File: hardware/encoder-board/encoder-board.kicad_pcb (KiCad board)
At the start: 4 copper layers, 25.4 x 25.4 mm, 26 parts, among them J1 Conn_01x04, U1 ITR1204SR10A_TR(BY), U2 ITR1204SR10A_TR(BY), U3 LM2903

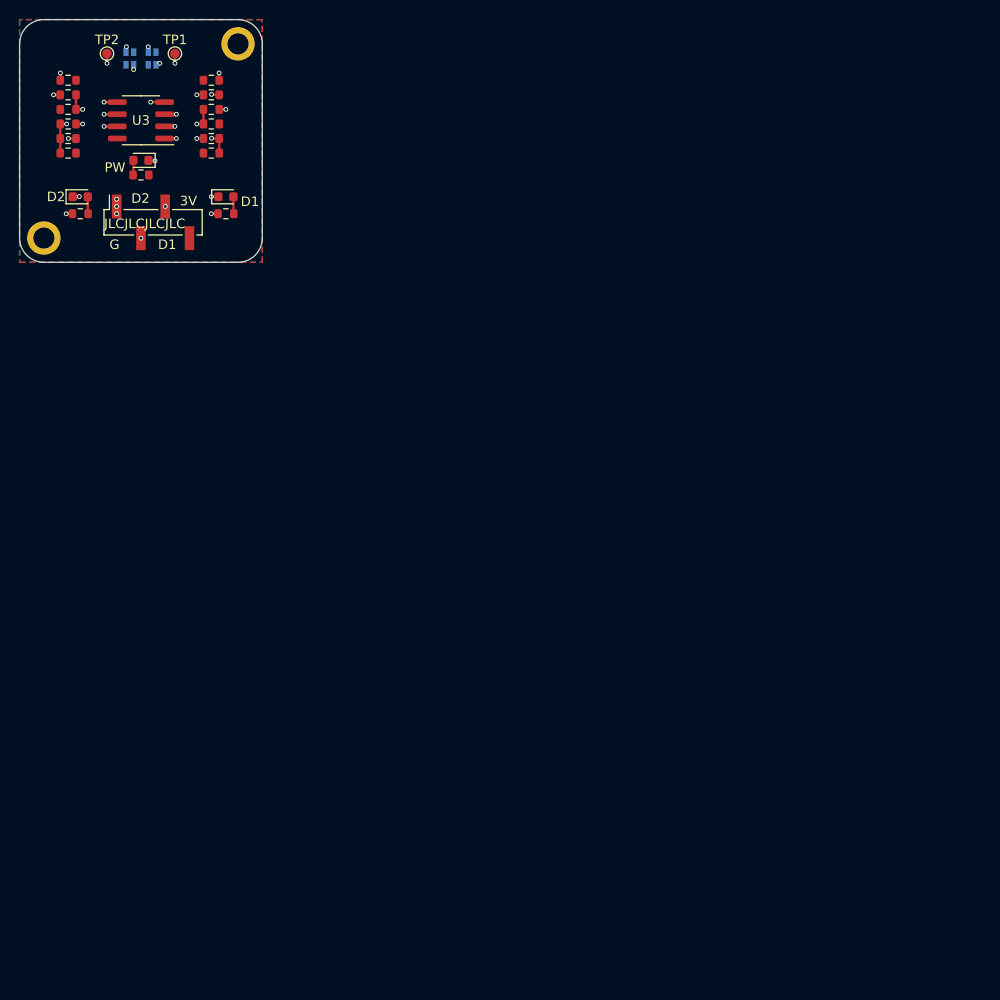
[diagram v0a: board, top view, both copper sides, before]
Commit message: remake encoder board pcb. generated jlcpcb production files.
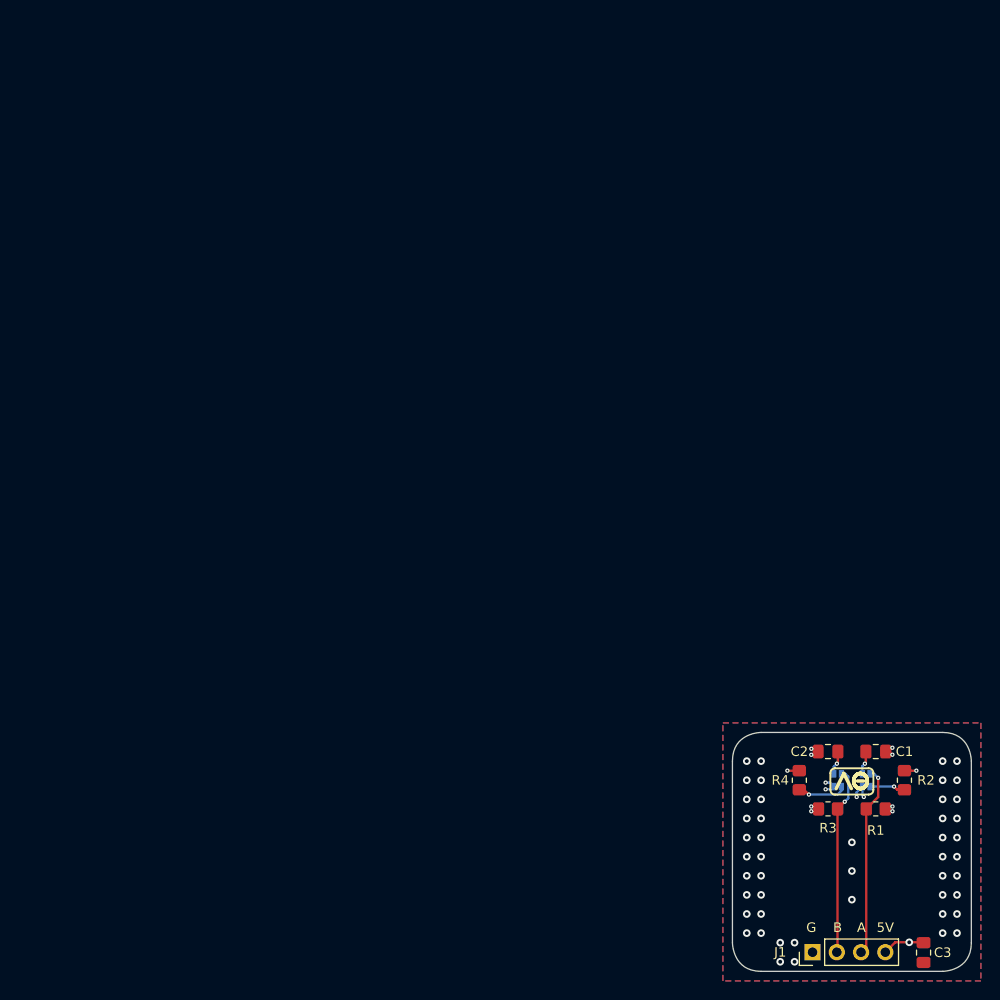
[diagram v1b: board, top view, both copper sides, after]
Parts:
- removed D1: Red, LED_SMD:LED_0603_1608Metric
- removed D2: Yellow, LED_SMD:LED_0603_1608Metric
- removed H1, H2: MountingHole_Pad, MountingHole:MountingHole_2.2mm_M2_ISO7380_Pad
- removed PW1: Green, LED_SMD:LED_0603_1608Metric
- removed R10, R11, R13, R14, R15, R8: 1k, Resistor_SMD:R_0603_1608Metric
- removed R12, R9: 1.5k, Resistor_SMD:R_0603_1608Metric
- removed R5: 30, Resistor_SMD:R_0603_1608Metric
- removed R6, R7: 130, Resistor_SMD:R_0603_1608Metric
- removed TP1, TP2: ~, TestPoint:TestPoint_Pad_D1.0mm
- removed U3: LM2903, Package_SO:SOIC-8_3.9x4.9mm_P1.27mm
- added C1: 100nF, Capacitor_SMD:C_0805_2012Metric_Pad1.18x1.45mm_HandSolder, F.Cu at (115.0, 102.0)
- added C2: 100nF, Capacitor_SMD:C_0805_2012Metric_Pad1.18x1.45mm_HandSolder, F.Cu at (110.0, 102.0)
- added C3: 10uF, Capacitor_SMD:C_0805_2012Metric_Pad1.18x1.45mm_HandSolder, F.Cu at (120.0, 123.0)
- J1: footprint Connector_PinHeader_2.54mm:PinHeader_1x04_P2.54mm_Vertical_SMD_Pin1Right -> Connector_PinHeader_2.54mm:PinHeader_1x04_P2.54mm_Vertical
- R1: value 1k -> 680; footprint Resistor_SMD:R_0603_1608Metric -> Resistor_SMD:R_0805_2012Metric_Pad1.20x1.40mm_HandSolder
- R2: renamed from R3; value 100 -> 390; footprint Resistor_SMD:R_0603_1608Metric -> Resistor_SMD:R_0805_2012Metric_Pad1.20x1.40mm_HandSolder
- R3: renamed from R2; value 1k -> 680; footprint Resistor_SMD:R_0603_1608Metric -> Resistor_SMD:R_0805_2012Metric_Pad1.20x1.40mm_HandSolder
- R4: value 100 -> 390; footprint Resistor_SMD:R_0603_1608Metric -> Resistor_SMD:R_0805_2012Metric_Pad1.20x1.40mm_HandSolder
- moved U1 106.3 mm to (114.0, 105.0), turned to 0 degrees
- moved R4 105.9 mm to (107.0, 105.0), turned to 90 degrees
- moved U2 105.8 mm to (111.0, 105.0), turned to 0 degrees
- moved R3 105.0 mm to (110.0, 108.0)
- moved R2 103.1 mm to (118.0, 105.0), turned to 90 degrees
- moved J1 102.9 mm to (108.4, 123.0)
- moved R1 97.7 mm to (115.0, 108.0)
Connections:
- J1 pad 2: D2 -> SENSE_B
- J1 pad 3: D1 -> SENSE_A
- J1 pad 4: +3V3 -> +5V
- R1 pad 1: +3V3 -> SENSE_A
- R1 pad 2: A1 -> GND
- R2 pad 2: +3V3 -> +5V
- R3 pad 1: +3V3 -> SENSE_B
- R3 pad 2: A2 -> GND
- R4 pad 2: +3V3 -> +5V
- U1 pad 1: A1 -> +5V
- U1 pad 2: GND -> SENSE_A
- U2 pad 1: A2 -> +5V
- U2 pad 2: GND -> SENSE_B
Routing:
- net D2: track 24.0 -> 0.00 mm, vias 4 -> 0
- net SENSE_A: track 0.00 -> 20.0 mm, vias 0 -> 1
- net SENSE_B: track 0.00 -> 19.7 mm, vias 0 -> 1
- net A2: track 18.2 -> 0.00 mm, vias 3 -> 0
- net D1: track 17.6 -> 0.00 mm, vias 4 -> 0
- net A1: track 16.9 -> 0.00 mm, vias 4 -> 0
- net +5V: track 0.00 -> 11.9 mm, vias 0 -> 5
- net GND: track 4.30 -> 11.3 mm, vias 9 -> 59
- net Net-(U1-A): track 10.4 -> 3.74 mm, vias 2 -> 1
- net Net-(U3B-+): track 6.16 -> 0.00 mm, vias 2 -> 0
- net Net-(U3A--): track 5.70 -> 0.00 mm, vias 2 -> 0
- net Net-(U2-A): track 10.4 -> 5.21 mm, vias 2 -> 1
- net Net-(U3A-+): track 4.91 -> 0.00 mm, vias 2 -> 0
- net Net-(U3B--): track 4.74 -> 0.00 mm, vias 2 -> 0
- net Net-(D2-A): track 1.79 -> 0.00 mm
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- added copper zone on In2.Cu, net +5V
- added copper zone on F.Cu, net GND
- added copper zone on In1.Cu, net GND
- removed copper zone on F.Cu, net +3V3
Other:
- board size 25.4 x 25.4 mm -> 25 x 25 mm
- board text added: "5V"
- board text added: "A"
- board text added: "B"
- board text added: "SNS_A"
- board text added: "SNS_B"
- board text removed: "3V"
- board text removed: "D1"
- board text removed: "D2"
- board text removed: "JLCJLCJLCJLC"
- board text removed: "PW"
